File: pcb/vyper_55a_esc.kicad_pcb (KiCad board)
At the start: 6 copper layers, 36 x 36 mm, 58 parts, among them Q1 Q_M1_A_HS, Q10 Q_M2_B_LS, Q11 Q_M2_C_HS, Q12 Q_M2_C_LS, Q13 Q_M3_A_HS, Q14 Q_M3_A_LS, Q15 Q_M3_B_HS, Q16 Q_M3_B_LS, Q17 Q_M3_C_HS, Q18 Q_M3_C_LS, Q19 Q_M4_A_HS, Q2 Q_M1_A_LS, Q20 Q_M4_A_LS, Q21 Q_M4_B_HS, Q22 Q_M4_B_LS, Q23 Q_M4_C_HS, Q24 Q_M4_C_LS, Q3 Q_M1_B_HS, Q4 Q_M1_B_LS, Q5 Q_M1_C_HS, Q6 Q_M1_C_LS, Q7 Q_M2_A_HS, Q8 Q_M2_A_LS, Q9 Q_M2_B_HS, U1 U_DRV_M1, U2 U_MCU_M1, U3 U_DRV_M2, U4 U_MCU_M2, U5 U_DRV_M3, U6 U_MCU_M3, U7 U_DRV_M4, U8 U_MCU_M4

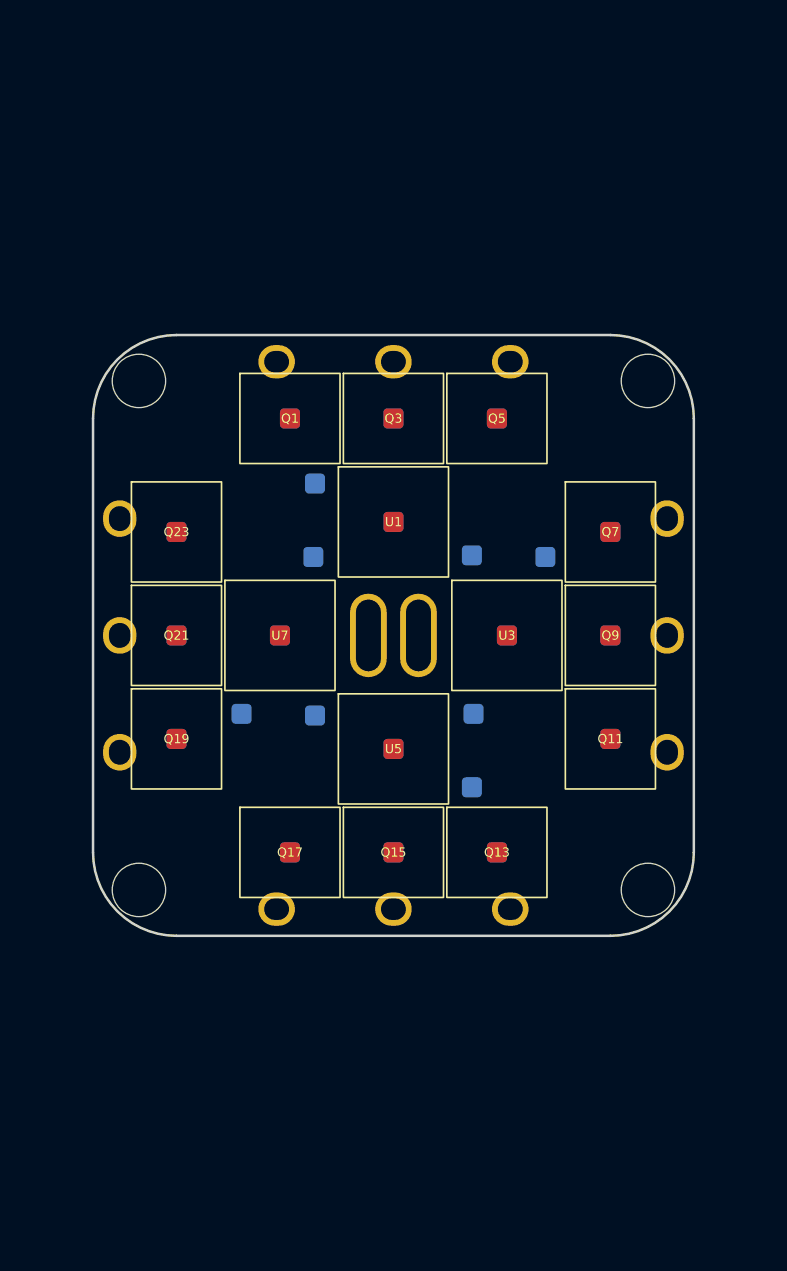
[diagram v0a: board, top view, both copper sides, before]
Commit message: Author VYPER four-channel ESC electrical checkpoint
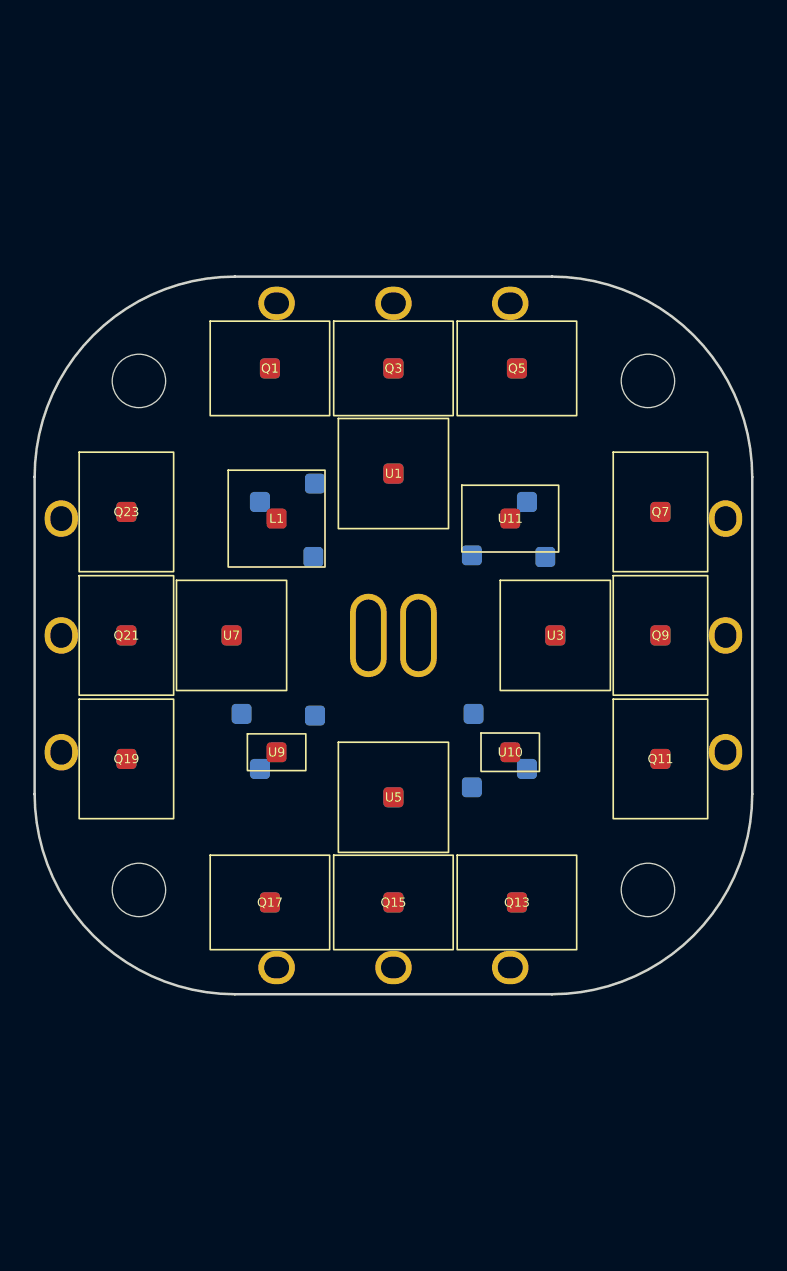
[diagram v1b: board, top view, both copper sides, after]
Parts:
- added L1: L_BUCK, VYPER_EVT:L_BUCK, F.Cu at (-7.00, -7.00)
- added RSH1: RSH_M1, VYPER_EVT:RSH_M1, B.Cu at (8.00, -8.00)
- added RSH2: RSH_M2, VYPER_EVT:RSH_M2, B.Cu at (8.00, 8.00)
- added RSH3: RSH_M3, VYPER_EVT:RSH_M3, B.Cu at (-8.00, 8.00)
- added RSH4: RSH_M4, VYPER_EVT:RSH_M4, B.Cu at (-8.00, -8.00)
- added U10: U_ISUM, VYPER_EVT:U_ISUM, F.Cu at (7.00, 7.00)
- added U11: J_HARNESS, VYPER_EVT:J_HARNESS, F.Cu at (7.00, -7.00)
- added U9: U_BUCK, VYPER_EVT:U_BUCK, F.Cu at (-7.00, 7.00)
- moved M1A 3.50 mm to (-7.00, -19.9)
- moved M1B 3.50 mm to (0.00, -19.9)
- moved M1C 3.50 mm to (7.00, -19.9)
- moved M2A 3.50 mm to (19.9, -7.00)
- moved M2B 3.50 mm to (19.9, -0.00)
- moved M2C 3.50 mm to (19.9, 7.00)
- moved M3A 3.50 mm to (7.00, 19.9)
- moved M3B 3.50 mm to (-0.00, 19.9)
- moved M3C 3.50 mm to (-7.00, 19.9)
- moved M4A 3.50 mm to (-19.9, 7.00)
- moved M4B 3.50 mm to (-19.9, -0.00)
- moved M4C 3.50 mm to (-19.9, -7.00)
- moved Q1 3.23 mm to (-7.40, -16.0)
- moved Q11 3.23 mm to (16.0, 7.40)
- moved Q12 3.23 mm to (16.0, 7.40)
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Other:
- board size 36 x 36 mm -> 43 x 43 mm

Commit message: Redesign VYPER around vertical dense electronics
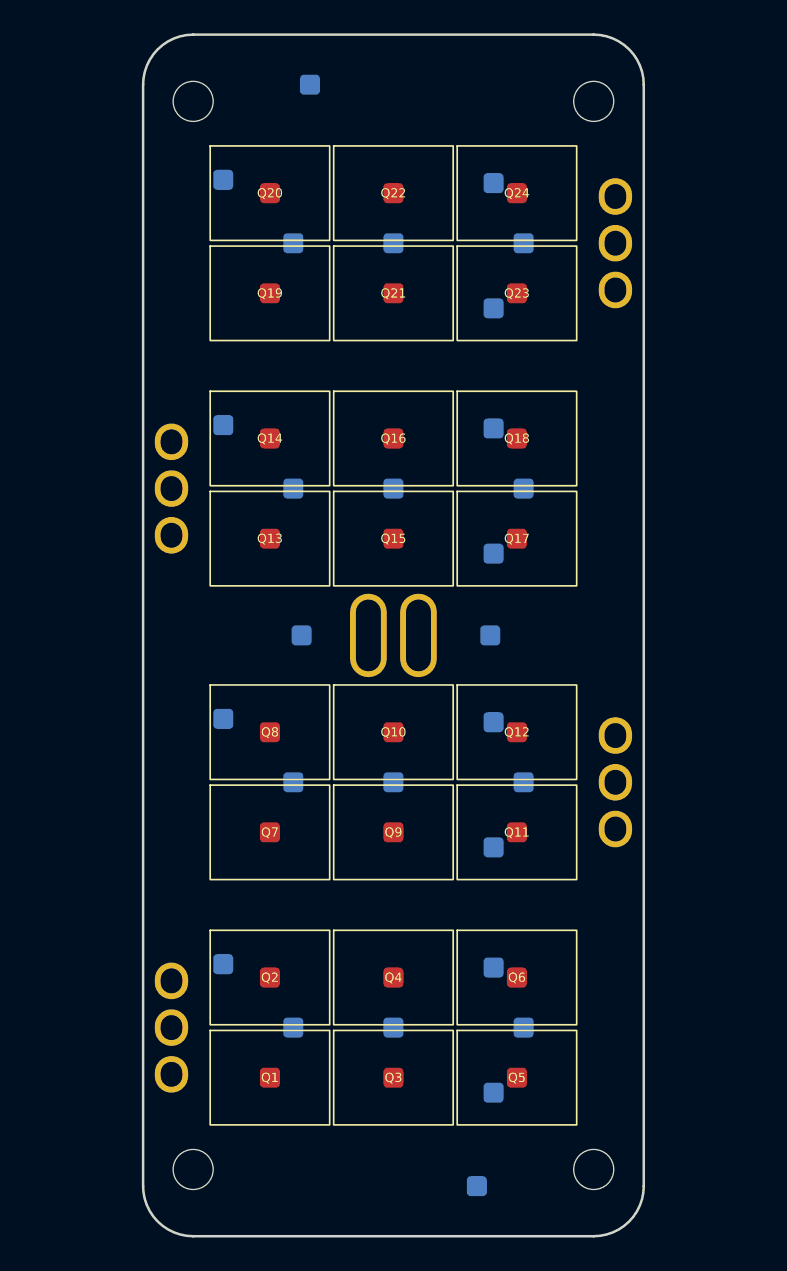
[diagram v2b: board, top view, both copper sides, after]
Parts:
- added U12: J_SWD_M1, VYPER_EVT:J_SWD_M1, B.Cu at (-10.2, 19.7)
- added U13: J_SWD_M2, VYPER_EVT:J_SWD_M2, B.Cu at (-10.2, 5.00)
- added U14: J_SWD_M3, VYPER_EVT:J_SWD_M3, B.Cu at (-10.2, -12.6)
- added U15: J_SWD_M4, VYPER_EVT:J_SWD_M4, B.Cu at (-10.2, -27.3)
- L1, U1, U10, U11, U3, U5, U7, U9: moved to B.Cu
- Q10, Q12, Q14, Q16, Q18, Q2, Q20, Q22, Q24, Q4, Q6, Q8: moved to F.Cu
- moved M1A 46.6 mm to (-13.3, 26.3)
- moved M1B 45.4 mm to (-13.3, 23.5)
- moved M1C 45.4 mm to (-13.3, 20.7)
- moved M4A 43.2 mm to (13.3, -20.7)
- moved Q1 42.5 mm to (-7.40, 26.5)
- moved Q3 42.5 mm to (0.00, 26.5)
- moved Q5 42.5 mm to (7.40, 26.5)
- moved U10 41.8 mm to (-5.00, -33.0)
- moved M4B 40.7 mm to (13.3, -23.5)
- moved U11 40.0 mm to (5.00, 33.0)
- moved M4C 38.4 mm to (13.3, -26.3)
- moved Q2 36.5 mm to (-7.40, 20.5)
- moved Q4 36.5 mm to (0.00, 20.5)
- moved Q6 36.5 mm to (7.40, 20.5)
- moved TH4 35.2 mm to (6.00, -27.1)
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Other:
- board size 43 x 43 mm -> 30 x 72 mm
- board text added: "VYPER-55A VERTICAL EVT / NOT FOR FAB"
- board text removed: "VYPER-55A EVT / NOT FOR FAB"

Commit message: Add production-size wire pads and reproducible PETG slicing
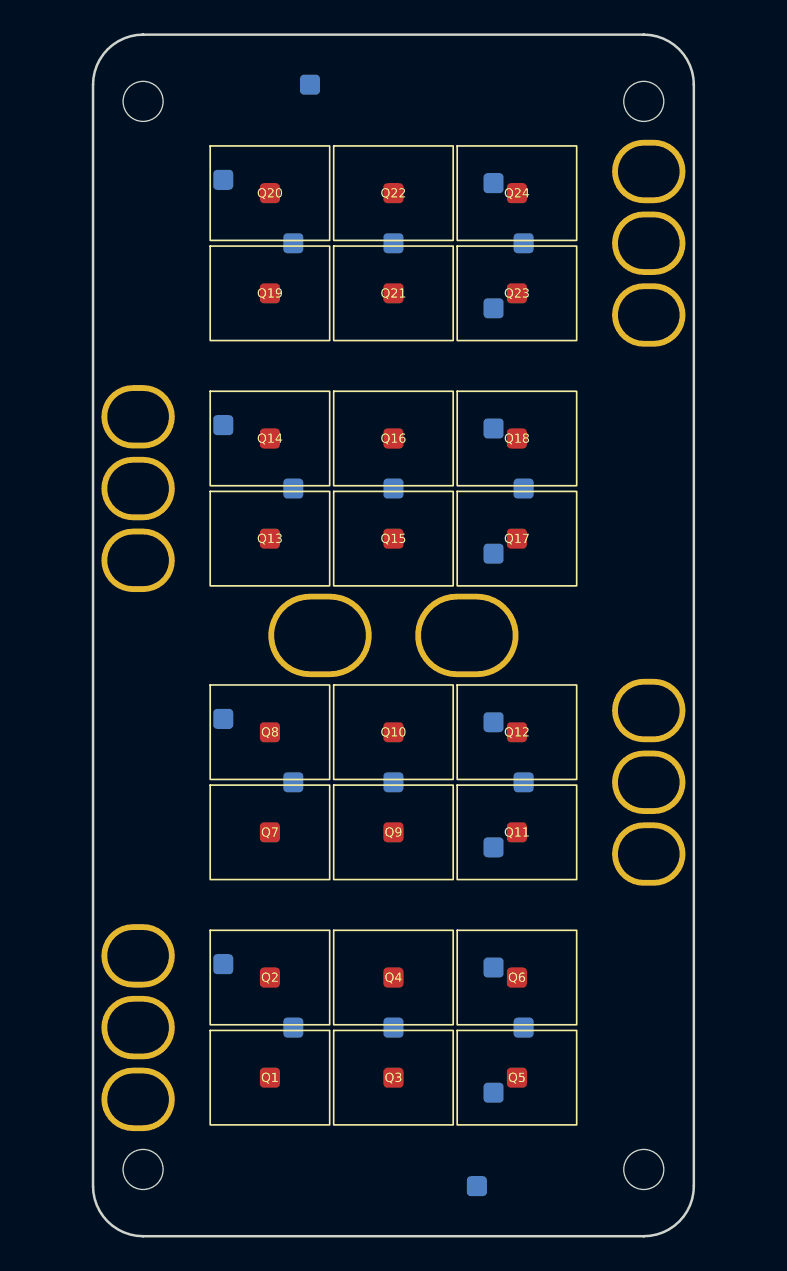
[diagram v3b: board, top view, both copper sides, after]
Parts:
- moved H1 3.00 mm to (-15.0, 32.0)
- moved H2 3.00 mm to (-15.0, -32.0)
- moved H3 3.00 mm to (15.0, 32.0)
- moved H4 3.00 mm to (15.0, -32.0)
- moved GND 2.90 mm to (4.40, -0.00)
- moved VBAT+ 2.90 mm to (-4.40, -0.00)
- moved M1A 2.50 mm to (-15.3, 27.8)
- moved M1C 2.50 mm to (-15.3, 19.2)
- moved M2A 2.50 mm to (15.3, 13.1)
- moved M2C 2.50 mm to (15.3, 4.50)
- moved M3A 2.50 mm to (-15.3, -4.50)
- moved M3C 2.50 mm to (-15.3, -13.1)
- moved M4A 2.50 mm to (15.3, -19.2)
- moved M4C 2.50 mm to (15.3, -27.8)
- moved M1B 2.00 mm to (-15.3, 23.5)
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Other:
- board size 30 x 72 mm -> 36 x 72 mm
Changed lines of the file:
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@@
 	(setup (pad_to_mask_clearance 0))
 	(net 0 "")
-	(gr_line (start -12.000 -36.000) (end 12.000 -36.000) (stroke (width 0.15) (type solid)) (layer "Edge.Cuts"))
-	(gr_line (start -12.000 36.000) (end 12.000 36.000) (stroke (width 0.15) (type solid)) (layer "Edge.Cuts"))
-	(gr_line (start -15.000 33.000) (end -15.000 -33.000) (stroke (width 0.15) (type solid)) (layer "Edge.Cuts"))
-	(gr_line (start 15.000 33.000) (end 15.000 -33.000) (stroke (width 0.15) (type solid)) (layer "Edge.Cuts"))
-	(gr_arc (start 15.000 -33.000) (mid 14.121 -35.121) (end 12.000 -36.000) (stroke (width 0.15) (type solid)) (layer "Edge.Cuts"))
-	(gr_arc (start -12.000 -36.000) (mid -14.121 -35.121) (end -15.000 -33.000) (stroke (width 0.15) (type solid)) (layer "Edge.Cuts"))
-	(gr_arc (start -15.000 33.000) (mid -14.121 35.121) (end -12.000 36.000) (stroke (width 0.15) (type solid)) (layer "Edge.Cuts"))
-	(gr_arc (start 12.000 36.000) (mid 14.121 35.121) (end 15.000 33.000) (stroke (width 0.15) (type solid)) (layer "Edge.Cuts"))
+	(gr_line (start -15.000 -36.000) (end 15.000 -36.000) (stroke (width 0.15) (type solid)) (layer "Edge.Cuts"))
+	(gr_line (start -15.000 36.000) (end 15.000 36.000) (stroke (width 0.15) (type solid)) (layer "Edge.Cuts"))
+	(gr_line (start -18.000 33.000) (end -18.000 -33.000) (stroke (width 0.15) (type solid)) (layer "Edge.Cuts"))
+	(gr_line (start 18.000 33.000) (end 18.000 -33.000) (stroke (width 0.15) (type solid)) (layer "Edge.Cuts"))
+	(gr_arc (start 18.000 -33.000) (mid 17.121 -35.121) (end 15.000 -36.000) (stroke (width 0.15) (type solid)) (layer "Edge.Cuts"))
+	(gr_arc (start -15.000 -36.000) (mid -17.121 -35.121) (end -18.000 -33.000) (stroke (width 0.15) (type solid)) (layer "Edge.Cuts"))
+	(gr_arc (start -18.000 33.000) (mid -17.121 35.121) (end -15.000 36.000) (stroke (width 0.15) (type solid)) (layer "Edge.Cuts"))
+	(gr_arc (start 15.000 36.000) (mid 17.121 35.121) (end 18.000 33.000) (stroke (width 0.15) (type solid)) (layer "Edge.Cuts"))
 	(footprint "VYPER_EVT:M3_CLEAR" (layer "F.Cu")
-		(at -12.000 32.000)
+		(at -15.000 32.000)
 		(property "Reference" "H1" (at 0 0 0) (layer "F.SilkS") hide (effects (font (size 0.5 0.5) (thickness 0.08))))
 		(pad "" np_thru_hole circle (at 0 0) (size 2.4 2.4) (drill 2.4) (layers "*.Cu" "*.Mask"))
 	)
 	(footprint "VYPER_EVT:M3_CLEAR" (layer "F.Cu")
-		(at -12.000 -32.000)
+		(at -15.000 -32.000)
 		(property "Reference" "H2" (at 0 0 0) (layer "F.SilkS") hide (effects (font (size 0.5 0.5) (thickness 0.08))))
 		(pad "" np_thru_hole circle (at 0 0) (size 2.4 2.4) (drill 2.4) (layers "*.Cu" "*.Mask"))
 	)
 	(footprint "VYPER_EVT:M3_CLEAR" (layer "F.Cu")
-		(at 12.000 32.000)
+		(at 15.000 32.000)
 		(property "Reference" "H3" (at 0 0 0) (layer "F.SilkS") hide (effects (font (size 0.5 0.5) (thickness 0.08))))
 		(pad "" np_thru_hole circle (at 0 0) (size 2.4 2.4) (drill 2.4) (layers "*.Cu" "*.Mask"))
 	)
 	(footprint "VYPER_EVT:M3_CLEAR" (layer "F.Cu")
-		(at 12.000 -32.000)
+		(at 15.000 -32.000)
 		(property "Reference" "H4" (at 0 0 0) (layer "F.SilkS") hide (effects (font (size 0.5 0.5) (thickness 0.08))))
 		(pad "" np_thru_hole circle (at 0 0) (size 2.4 2.4) (drill 2.4) (layers "*.Cu" "*.Mask"))
@@
 	)
 	(footprint "VYPER_EVT:M1_A" (layer "F.Cu")
-		(at -13.300 26.300)
+		(at -15.300 27.800)
 		(attr exclude_from_bom exclude_from_pos_files)
 		(property "Reference" "M1A" (at 0 0 0) (layer "F.SilkS") hide (effects (font (size 0.5 0.5) (thickness 0.08))))
-		(pad "1" thru_hole oval (at 0 0) (size 2.00 2.20) (drill oval 1.30 1.50) (layers "*.Cu" "*.Mask"))
+		(pad "1" thru_hole oval (at 0 0) (size 4.40 3.80) (drill oval 3.70 3.10) (layers "*.Cu" "*.Mask"))
 	)
 	(footprint "VYPER_EVT:M1_B" (layer "F.Cu")
-		(at -13.300 23.500)
+		(at -15.300 23.500)
 		(attr exclude_from_bom exclude_from_pos_files)
 		(property "Reference" "M1B" (at 0 0 0) (layer "F.SilkS") hide (effects (font (size 0.5 0.5) (thickness 0.08))))
-		(pad "1" thru_hole oval (at 0 0) (size 2.00 2.20) (drill oval 1.30 1.50) (layers "*.Cu" "*.Mask"))
+		(pad "1" thru_hole oval (at 0 0) (size 4.40 3.80) (drill oval 3.70 3.10) (layers "*.Cu" "*.Mask"))
 	)
 	(footprint "VYPER_EVT:M1_C" (layer "F.Cu")
-		(at -13.300 20.700)
+		(at -15.300 19.200)
 		(attr exclude_from_bom exclude_from_pos_files)
 		(property "Reference" "M1C" (at 0 0 0) (layer "F.SilkS") hide (effects (font (size 0.5 0.5) (thickness 0.08))))
-		(pad "1" thru_hole oval (at 0 0) (size 2.00 2.20) (drill oval 1.30 1.50) (layers "*.Cu" "*.Mask"))
+		(pad "1" thru_hole oval (at 0 0) (size 4.40 3.80) (drill oval 3.70 3.10) (layers "*.Cu" "*.Mask"))
 	)
 	(footprint "VYPER_EVT:M2_A" (layer "F.Cu")
-		(at 13.300 11.600)
+		(at 15.300 13.100)
 		(attr exclude_from_bom exclude_from_pos_files)
 		(property "Reference" "M2A" (at 0 0 0) (layer "F.SilkS") hide (effects (font (size 0.5 0.5) (thickness 0.08))))
-		(pad "1" thru_hole oval (at 0 0) (size 2.00 2.20) (drill oval 1.30 1.50) (layers "*.Cu" "*.Mask"))
+		(pad "1" thru_hole oval (at 0 0) (size 4.40 3.80) (drill oval 3.70 3.10) (layers "*.Cu" "*.Mask"))
 	)
 	(footprint "VYPER_EVT:M2_B" (layer "F.Cu")
-		(at 13.300 8.800)
+		(at 15.300 8.800)
 		(attr exclude_from_bom exclude_from_pos_files)
 		(property "Reference" "M2B" (at 0 0 0) (layer "F.SilkS") hide (effects (font (size 0.5 0.5) (thickness 0.08))))
-		(pad "1" thru_hole oval (at 0 0) (size 2.00 2.20) (drill oval 1.30 1.50) (layers "*.Cu" "*.Mask"))
+		(pad "1" thru_hole oval (at 0 0) (size 4.40 3.80) (drill oval 3.70 3.10) (layers "*.Cu" "*.Mask"))
 	)
 	(footprint "VYPER_EVT:M2_C" (layer "F.Cu")
-		(at 13.300 6.000)
+		(at 15.300 4.500)
 		(attr exclude_from_bom exclude_from_pos_files)
 		(property "Reference" "M2C" (at 0 0 0) (layer "F.SilkS") hide (effects (font (size 0.5 0.5) (thickness 0.08))))
-		(pad "1" thru_hole oval (at 0 0) (size 2.00 2.20) (drill oval 1.30 1.50) (layers "*.Cu" "*.Mask"))
+		(pad "1" thru_hole oval (at 0 0) (size 4.40 3.80) (drill oval 3.70 3.10) (layers "*.Cu" "*.Mask"))
 	)
 	(footprint "VYPER_EVT:M3_A" (layer "F.Cu")
-		(at -13.300 -6.000)
+		(at -15.300 -4.500)
 		(attr exclude_from_bom exclude_from_pos_files)
 		(property "Reference" "M3A" (at 0 0 0) (layer "F.SilkS") hide (effects (font (size 0.5 0.5) (thickness 0.08))))
-		(pad "1" thru_hole oval (at 0 0) (size 2.00 2.20) (drill oval 1.30 1.50) (layers "*.Cu" "*.Mask"))
+		(pad "1" thru_hole oval (at 0 0) (size 4.40 3.80) (drill oval 3.70 3.10) (layers "*.Cu" "*.Mask"))
 	)
 	(footprint "VYPER_EVT:M3_B" (layer "F.Cu")
-		(at -13.300 -8.800)
+		(at -15.300 -8.800)
 		(attr exclude_from_bom exclude_from_pos_files)
 		(property "Reference" "M3B" (at 0 0 0) (layer "F.SilkS") hide (effects (font (size 0.5 0.5) (thickness 0.08))))
-		(pad "1" thru_hole oval (at 0 0) (size 2.00 2.20) (drill oval 1.30 1.50) (layers "*.Cu" "*.Mask"))
+		(pad "1" thru_hole oval (at 0 0) (size 4.40 3.80) (drill oval 3.70 3.10) (layers "*.Cu" "*.Mask"))
 	)
 	(footprint "VYPER_EVT:M3_C" (layer "F.Cu")
-		(at -13.300 -11.600)
+		(at -15.300 -13.100)
 		(attr exclude_from_bom exclude_from_pos_files)
 		(property "Reference" "M3C" (at 0 0 0) (layer "F.SilkS") hide (effects (font (size 0.5 0.5) (thickness 0.08))))
-		(pad "1" thru_hole oval (at 0 0) (size 2.00 2.20) (drill oval 1.30 1.50) (layers "*.Cu" "*.Mask"))
+		(pad "1" thru_hole oval (at 0 0) (size 4.40 3.80) (drill oval 3.70 3.10) (layers "*.Cu" "*.Mask"))
 	)
 	(footprint "VYPER_EVT:M4_A" (layer "F.Cu")
-		(at 13.300 -20.700)
+		(at 15.300 -19.200)
 		(attr exclude_from_bom exclude_from_pos_files)
 		(property "Reference" "M4A" (at 0 0 0) (layer "F.SilkS") hide (effects (font (size 0.5 0.5) (thickness 0.08))))
-		(pad "1" thru_hole oval (at 0 0) (size 2.00 2.20) (drill oval 1.30 1.50) (layers "*.Cu" "*.Mask"))
+		(pad "1" thru_hole oval (at 0 0) (size 4.40 3.80) (drill oval 3.70 3.10) (layers "*.Cu" "*.Mask"))
 	)
 	(footprint "VYPER_EVT:M4_B" (layer "F.Cu")
-		(at 13.300 -23.500)
+		(at 15.300 -23.500)
 		(attr exclude_from_bom exclude_from_pos_files)
 		(property "Reference" "M4B" (at 0 0 0) (layer "F.SilkS") hide (effects (font (size 0.5 0.5) (thickness 0.08))))
-		(pad "1" thru_hole oval (at 0 0) (size 2.00 2.20) (drill oval 1.30 1.50) (layers "*.Cu" "*.Mask"))
+		(pad "1" thru_hole oval (at 0 0) (size 4.40 3.80) (drill oval 3.70 3.10) (layers "*.Cu" "*.Mask"))
 	)
 	(footprint "VYPER_EVT:M4_C" (layer "F.Cu")
-		(at 13.300 -26.300)
+		(at 15.300 -27.800)
 		(attr exclude_from_bom exclude_from_pos_files)
 		(property "Reference" "M4C" (at 0 0 0) (layer "F.SilkS") hide (effects (font (size 0.5 0.5) (thickness 0.08))))
-		(pad "1" thru_hole oval (at 0 0) (size 2.00 2.20) (drill oval 1.30 1.50) (layers "*.Cu" "*.Mask"))
+		(pad "1" thru_hole oval (at 0 0) (size 4.40 3.80) (drill oval 3.70 3.10) (layers "*.Cu" "*.Mask"))
 	)
 	(footprint "VYPER_EVT:VBAT+" (layer "F.Cu")
-		(at -1.500 -0.000)
+		(at -4.400 -0.000)
 		(attr exclude_from_bom exclude_from_pos_files)
 		(property "Reference" "VBAT+" (at 0 0 0) (layer "F.SilkS") hide (effects (font (size 0.5 0.5) (thickness 0.08))))
-		(pad "1" thru_hole oval (at 0 0) (size 2.20 5.00) (drill oval 1.50 4.30) (layers "*.Cu" "*.Mask"))
+		(pad "1" thru_hole oval (at 0 0) (size 6.20 5.00) (drill oval 5.50 4.30) (layers "*.Cu" "*.Mask"))
 	)
 	(footprint "VYPER_EVT:GND" (layer "F.Cu")
-		(at 1.500 -0.000)
+		(at 4.400 -0.000)
 		(attr exclude_from_bom exclude_from_pos_files)
 		(property "Reference" "GND" (at 0 0 0) (layer "F.SilkS") hide (effects (font (size 0.5 0.5) (thickness 0.08))))
-		(pad "1" thru_hole oval (at 0 0) (size 2.20 5.00) (drill oval 1.50 4.30) (layers "*.Cu" "*.Mask"))
+		(pad "1" thru_hole oval (at 0 0) (size 6.20 5.00) (drill oval 5.50 4.30) (layers "*.Cu" "*.Mask"))
 	)
 	(gr_text "VYPER-55A VERTICAL EVT / NOT FOR FAB" (at 0 0 0) (layer "Dwgs.User") (effects (font (size 1.0 1.0) (thickness 0.15))))
